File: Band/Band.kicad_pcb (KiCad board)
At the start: 2 copper layers, 36 parts, among them J1 USB_C_Receptacle_USB2.0, U1 ESP32-C3-WROOM-02, U2 TC2014-1.8VxCTTR, U3 BMP280, U4 BMI270, U5 MAX30102, U6 BQ25504, U7 S-1318A33

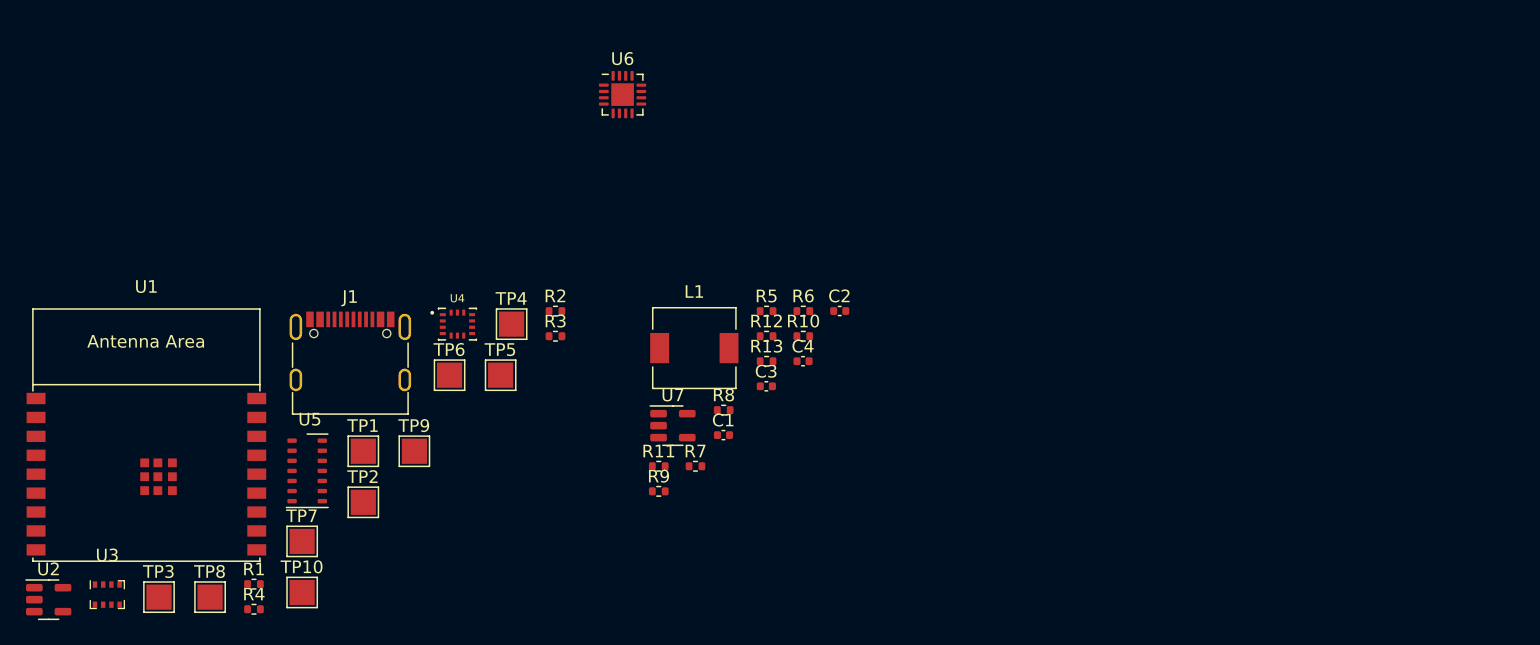
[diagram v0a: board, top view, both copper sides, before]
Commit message: preliminary layout
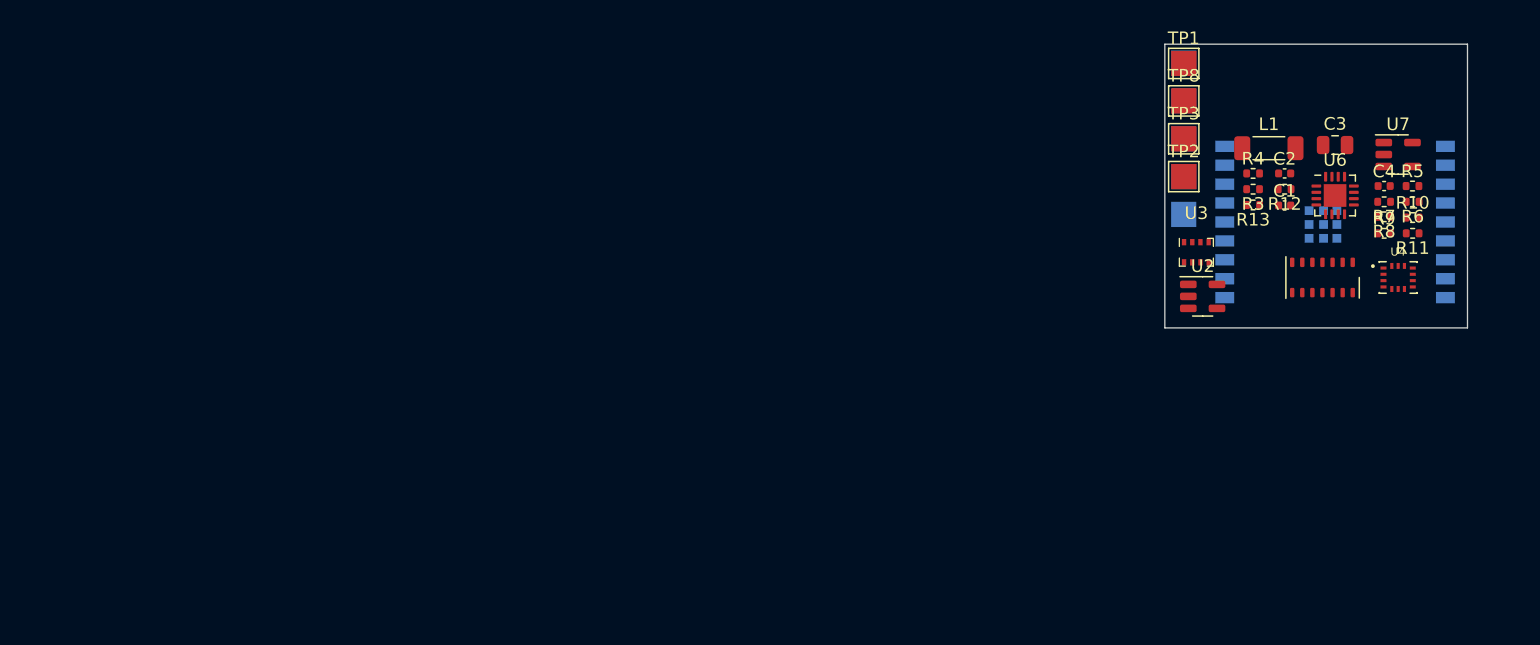
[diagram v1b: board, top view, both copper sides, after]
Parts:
- removed J1: USB_C_Receptacle_USB2.0, Connector_USB:USB_C_Receptacle_G-Switch_GT-USB-7010ASV
- removed R1, R2: 5.1k, Resistor_SMD:R_0402_1005Metric
- removed TP10: BATT, TestPoint:TestPoint_Pad_2.0x2.0mm
- removed TP4: PV, TestPoint:TestPoint_Pad_2.0x2.0mm
- removed TP9: GND, TestPoint:TestPoint_Pad_2.0x2.0mm
- added TP11: D-, TestPoint:TestPoint_Pad_2.0x2.0mm, B.Cu at (165.5, 47.5)
- added TP12: D+, TestPoint:TestPoint_Pad_2.0x2.0mm, B.Cu at (165.5, 50.5)
- C1: value C_Small -> Cref
- C3: footprint Capacitor_SMD:C_0402_1005Metric -> Capacitor_SMD:C_0805_2012Metric
- L1: footprint Inductor_SMD:L_6.3x6.3_H3 -> Inductor_SMD:L_1806_4516Metric
- R10: value Rov2 -> Ruv2
- R11: value Rov1 -> Ruv1
- TP5, TP6, TP7, U1: moved to B.Cu
- moved U1 96.4 mm to (177.5, 57.0), turned to 180 degrees
- moved U2 94.6 mm to (167.0, 63.0)
- moved U3 90.5 mm to (166.5, 59.5)
- moved TP3 89.0 mm to (165.5, 50.5)
- moved TP8 86.7 mm to (165.5, 47.5)
- moved R4 86.4 mm to (171.0, 53.2)
- moved U5 82.0 mm to (176.5, 61.5), turned to -90 degrees
- moved U4 74.7 mm to (182.5, 61.5)
- moved TP7 74.6 mm to (165.5, 56.5), turned to 180 degrees
- moved TP1 72.0 mm to (165.5, 44.5)
- moved TP2 70.0 mm to (165.5, 53.5)
- moved TP6 63.3 mm to (165.5, 44.5), turned to 180 degrees
- moved R11 62.6 mm to (183.7, 58.0), turned to 180 degrees
- moved U7 61.4 mm to (182.5, 51.8)
- moved R9 61.1 mm to (181.4, 58.0)
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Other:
- board outline added: 24 x 22.5 mm

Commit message: finish layout and route
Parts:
- moved U3 17.9 mm to (184.2, 62.0)
- moved U5 8.25 mm to (168.2, 61.8)
- moved U2 7.71 mm to (174.6, 61.8)
- moved U4 3.04 mm to (179.5, 62.0)
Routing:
- net GND: track 0.00 -> 42.7 mm, vias 0 -> 21
- net Net-(U2-Pad5): track 0.00 -> 26.5 mm, vias 0 -> 2
- net /Power_Management/BATT: track 0.00 -> 25.8 mm
- net Net-(U1-Pad3): track 0.00 -> 23.1 mm, vias 0 -> 1
- net SPI_MISO: track 0.00 -> 21.4 mm, vias 0 -> 1
- net Net-(U1-Pad7): track 0.00 -> 21.1 mm, vias 0 -> 1
- net SCL: track 0.00 -> 20.9 mm, vias 0 -> 3
- net /Power_Management/PV: track 0.00 -> 18.0 mm
- net Net-(U1-Pad15): track 0.00 -> 17.6 mm, vias 0 -> 1
- net SDA: track 0.00 -> 17.3 mm, vias 0 -> 1
- net Net-(U1-Pad13): track 0.00 -> 14.8 mm
- net Net-(TP7-Pad1): track 0.00 -> 11.3 mm
- net Net-(TP5-Pad1): track 0.00 -> 10.7 mm
- net Net-(R10-Pad2): track 0.00 -> 9.95 mm, vias 0 -> 2
- net Net-(U1-Pad14): track 0.00 -> 8.68 mm
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- added copper zone on B.Cu, net +3.3V
- added copper zone on In1.Cu, net +3.3V
- added copper zone on F.Cu, net GND
- added copper zone on In2.Cu, net GND
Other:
- copper layers 2 -> 4

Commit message: v1 final changes
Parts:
- L1: footprint Inductor_SMD:L_1806_4516Metric -> Inductor_SMD:L_1210_3225Metric
- moved L1 0.25 mm to (172.2, 51.0)
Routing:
- net /Power_Management/BATT: track 25.8 -> 55.4 mm, vias 0 -> 2
- net Net-(L1-Pad2): track 3.32 -> 4.27 mm
